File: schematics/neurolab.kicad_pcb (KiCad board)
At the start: 2 copper layers, 127 x 53.6 mm, 159 parts, among them J1 GS3, J10 GS3, J12 GS3, J13 GS3, J14 GS3, J15 GS3, J16 Channel, J17 External, J18 USB_OTG, J19 GS3, J2 GS3, J24 GS2, J3 GS3, J32 Bluetooth, J33 Reset Select, J34 GS2, J4 GS2, J5 GS2, J6 GS3, J7 GS3, J8 PowerOut, J9 GS3, Q1 2N7002, U1 ADP1720ARMZ-5, U10 OPA2111KP, U11 AD8422ARMZ, U12 OP4117, U13 OPA2111KP, U14 AD8422ARMZ, U15 OP4117, U16 AD7173, U17 ADR445BR, U18 Arduino, U2 ADP1720ARMZ-3.3, U3 AD8475, U4 AD8475, U5 MAX7480ESA+, U6 MAX7480ESA+, U7 MAX7480ESA+, U8 MAX7480ESA+, U9 TLC555CD, Y1 FA-20H

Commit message: optimize: final routing
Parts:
- removed J33: Reset Select, Connectors:GS3
- removed U18: Arduino, Pin_Headers:Pin_Header_Straight_2x12_Pitch2.54mm
- added J11: ProMini, Pin_Headers:Pin_Header_Straight_2x07_Pitch2.54mm, F.Cu at (179.8, 84.8)
- J32: footprint Pin_Headers:Pin_Header_Straight_1x06_Pitch2.54mm -> Pin_Headers:Pin_Header_Straight_1x04_Pitch2.54mm
- J34, J4, J5: moved to B.Cu
- moved J32 38.0 mm to (174.8, 80.9)
- moved J5 34.4 mm to (156.2, 101.9), turned to 0 degrees
- moved J4 34.0 mm to (156.4, 85.7), turned to 0 degrees
- moved J34 20.8 mm to (183.0, 104.9), turned to 0 degrees
- moved D2 19.3 mm to (183.4, 113.7)
- moved R44 17.6 mm to (183.4, 109.3), turned to 270 degrees
- moved R50 5.38 mm to (169.6, 79.8)
- moved R46 5.12 mm to (164.6, 82.2)
- moved R45 5.04 mm to (164.6, 79.8)
- moved R49 4.95 mm to (169.6, 82.2)
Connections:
- J32 pad 1: (no net) -> VCC
- J32 pad 2: VCC -> GND
- J32 pad 3: GND -> TxO
- J32 pad 4: TxO -> RxI
- R44 pad 1: Net-(D2-Pad2) -> Net-(J11-Pad12)
- R44 pad 2: Net-(R44-Pad2) -> Net-(D2-Pad2)
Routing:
- net Net-(J33-Pad1): track 80.7 -> 0.00 mm, vias 1 -> 0
- net AD3: track 110.3 -> 50.9 mm
- net Net-(J33-Pad3): track 49.6 -> 0.00 mm
- net GND: track 225.7 -> 186.9 mm, vias 57 -> 58
- net VCC: track 3.28 -> 39.2 mm, vias 0 -> 1
- net AD1: track 27.7 -> 62.5 mm, vias 0 -> 2
- net AD0: track 25.5 -> 59.0 mm, vias 0 -> 3
- net MOSI: track 5.02 -> 33.9 mm
- net CS: track 2.54 -> 29.0 mm, vias 0 -> 2
- net Net-(R44-Pad2): track 23.3 -> 0.00 mm, vias 2 -> 0
- net SCL: track 0.00 -> 19.6 mm, vias 0 -> 2
- net AD2: track 56.5 -> 40.5 mm, vias 0 -> 2
- net /ADConverter/DI: track 5.90 -> 20.1 mm
- net /ADConverter/SCL: track 6.64 -> 19.7 mm
- net Net-(J11-Pad12): track 0.00 -> 11.9 mm
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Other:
- board size 127 x 53.6 mm -> 93.4 x 38.3 mm

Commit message: feat: schematics and readme update
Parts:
- added C64: 100u, Capacitors_Tantalum_SMD:CP_Tantalum_Case-C_EIA-6032-28_Reflow, F.Cu at (96.8, 118.6)
- added C65: 100u, Capacitors_Tantalum_SMD:CP_Tantalum_Case-C_EIA-6032-28_Reflow, F.Cu at (96.7, 130.4)
- added C66: 100u, Capacitors_Tantalum_SMD:CP_Tantalum_Case-C_EIA-6032-28_Reflow, F.Cu at (105.3, 130.4)
- added C67: 100u, Capacitors_Tantalum_SMD:CP_Tantalum_Case-C_EIA-6032-28_Reflow, F.Cu at (105.3, 118.7)
- added C68: 100u, Capacitors_Tantalum_SMD:CP_Tantalum_Case-C_EIA-6032-28_Reflow, F.Cu at (113.9, 130.4)
- added C69: 100u, Capacitors_Tantalum_SMD:CP_Tantalum_Case-C_EIA-6032-28_Reflow, F.Cu at (113.9, 118.6)
- added G***: LOGO, Neuro:Logo, F.Cu at (173.6, 90.7)
- added G***: LOGO, Neuro:QR, B.Cu at (130.2, 97.8)
- added JP1: VoltOut, Connectors:GS3, B.Cu at (114.0, 124.4)
- added JP2: VVV, Connectors:GS3, B.Cu at (109.2, 124.4)
- added REF***: ESD-Logo_8.9x8mm_SilkScreen, Symbols:ESD-Logo_8.9x8mm_SilkScreen, B.Cu at (170.4, 111.0)
- added REF***: OSHW-Logo_5.7x6mm_SilkScreen, Symbols:OSHW-Logo_5.7x6mm_SilkScreen, B.Cu at (100.4, 127.3)
- added REF***: WEEE-Logo_5.6x8mm_SilkScreen, Symbols:WEEE-Logo_5.6x8mm_SilkScreen, B.Cu at (179.8, 111.7)
- added U18: TC1240A, TO_SOT_Packages_SMD:SOT-23-6, F.Cu at (96.8, 124.6)
- added U19: TC1240A, TO_SOT_Packages_SMD:SOT-23-6, F.Cu at (105.3, 124.6)
- added U20: 7660, Housings_SOIC:SOIC-8_3.9x4.9mm_Pitch1.27mm, F.Cu at (113.9, 124.5)
- J16: moved to B.Cu
- J8: value PowerOut -> 5.5V; footprint Pin_Headers:Pin_Header_Straight_2x02_Pitch2.54mm -> Pin_Headers:Pin_Header_Straight_1x01_Pitch2.54mm
- moved J8 24.3 mm to (117.1, 112.0)
- moved J16 12.7 mm to (95.7, 90.7)
- moved J18 1.50 mm to (94.6, 83.0)
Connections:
- J16 pad 1: /Amplifier Block 2/IN+ -> /Amplifier Block 1/IN-
- J16 pad 2: /Amplifier Block 2/IN- -> /Amplifier Block 1/IN+
- J16 pad 5: /Amplifier Block 1/IN+ -> /Amplifier Block 2/IN-
- J16 pad 6: /Amplifier Block 1/IN- -> /Amplifier Block 2/IN+
- J8 pad 1: -12V -> +5.5V
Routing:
- net +5V: track 192.1 -> 264.2 mm, vias 14 -> 17
- net Net-(C65-Pad1): track 0.00 -> 32.8 mm, vias 0 -> 1
- net -12V: track 152.2 -> 175.0 mm, vias 7 -> 9
- net +5.5V: track 148.7 -> 126.4 mm, vias 3 -> 2
- net Net-(C67-Pad1): track 0.00 -> 17.4 mm, vias 0 -> 1
- net Net-(C21-Pad3): track 34.7 -> 20.1 mm, vias 0 -> 1
- net Net-(C20-Pad3): track 33.2 -> 21.1 mm, vias 0 -> 1
- net +12V: track 162.0 -> 173.2 mm
- net Net-(C66-Pad1): track 0.00 -> 8.05 mm
- net Net-(C64-Pad2): track 0.00 -> 8.05 mm
- net Net-(C64-Pad1): track 0.00 -> 6.05 mm
- net Net-(C66-Pad2): track 0.00 -> 5.99 mm
- net Net-(C68-Pad1): track 0.00 -> 4.95 mm
- net Net-(JP2-Pad2): track 0.00 -> 4.89 mm, vias 0 -> 1
- net GND: track 186.9 -> 182.4 mm, vias 58 -> 64
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- added copper zone on F.Cu, net (none)
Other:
- board size 93.4 x 38.3 mm -> 93.6 x 55 mm
- board text added: "+12 OUT 5.5V"
- board text added: "+5.5V"
- board text added: "+5V"
- board text added: "+5V VCO 5.5V"
- board text added: "AD0"
- board text added: "AD1"
- board text added: "AD2"
- board text added: "AD2 GND"
- board text added: "AD3"
- board text added: "AD3 CPG"
- board text added: "AVC VCC"
- board text added: "CLK"
- board text added: "CS"
- board text added: "GND"
- board text added: "I1+ I1- GND GND I2+ I2-"
- board text added: "ICL CLK ECL"
- board text added: "IN+ IN+ OUT"
- board text added: "IN+ OU- OUT"
- board text added: "IN- OU- OUT"
- board text added: "LED"
- board text added: "MISO"
- board text added: "MOSI"
- board text added: "NeuroLab V1.0 Experimental Design"
- board text added: "OUT IN- IN-"
- board text added: "Rx"
- board text added: "SCL"
- board text added: "Sx1 +12 Sx2"
- board text added: "Tx"
- board text added: "USB +5V EXT"
- board text added: "VCC"
- board text added: "VCO A13"
- board text added: "VLO OUT VLH"

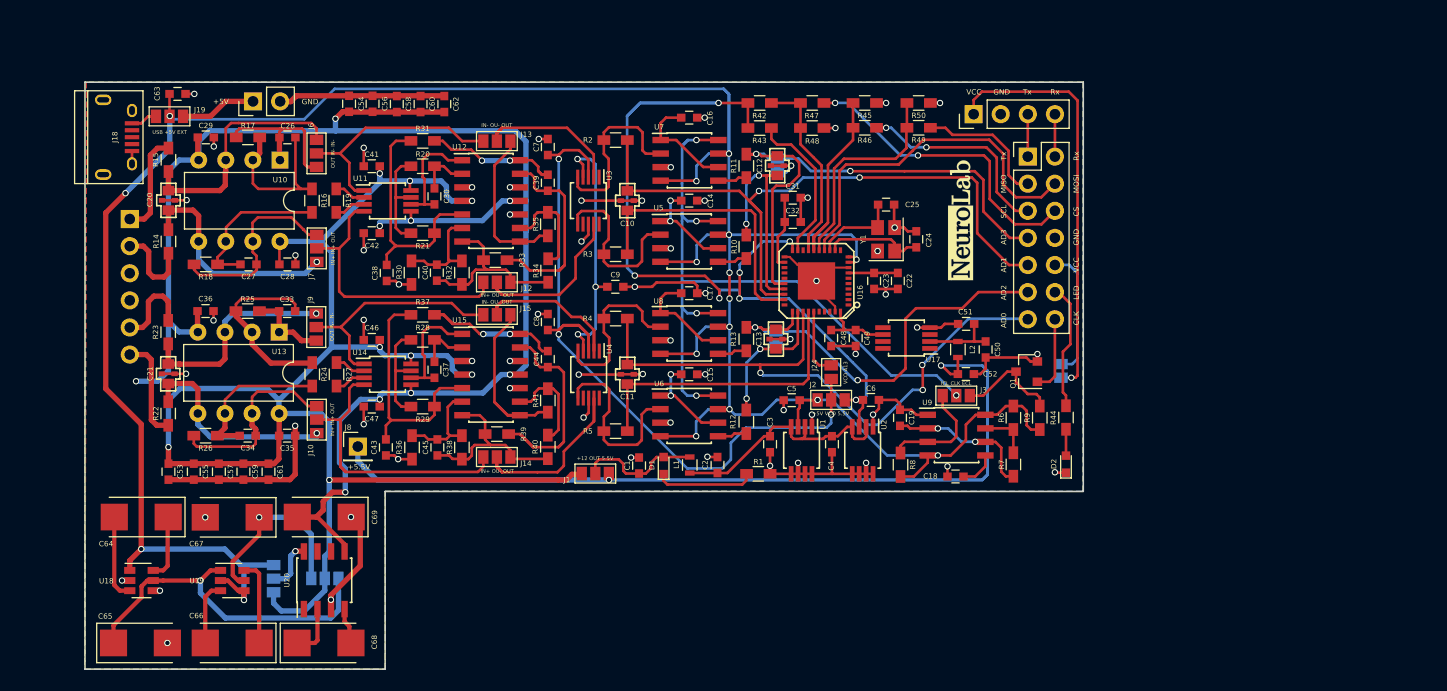
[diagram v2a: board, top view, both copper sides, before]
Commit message: Optimized Routing and Fixed DRC
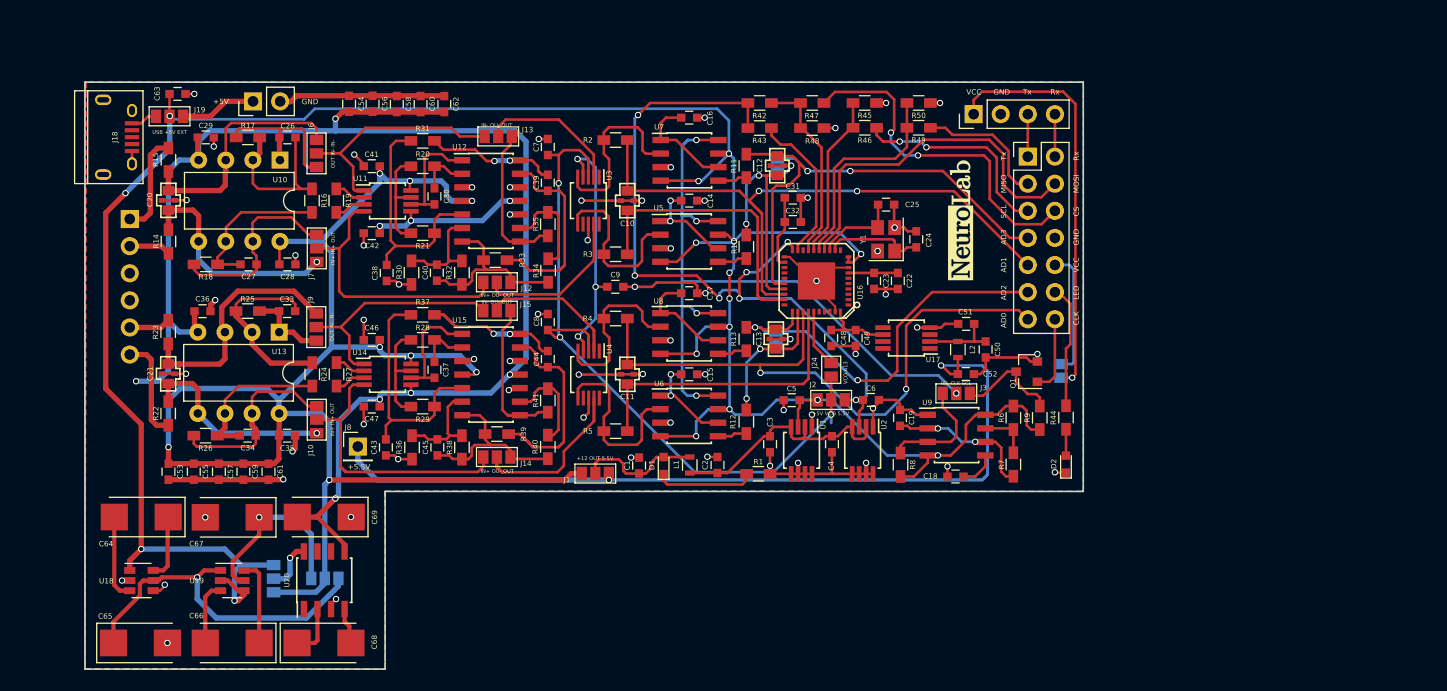
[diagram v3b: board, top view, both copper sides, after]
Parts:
- moved J13 0.46 mm to (130.2, 83.0)
- moved J15 0.39 mm to (130.1, 99.3)
- moved C36 0.29 mm to (102.5, 99.3)
- moved J24 0.22 mm to (161.4, 104.8)
- moved J3 0.21 mm to (173.2, 107.0)
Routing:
- net GND: track 182.4 -> 163.5 mm, vias 64 -> 65
- net +3V: track 88.4 -> 75.9 mm
- net -12V: track 175.0 -> 165.2 mm
- net +5V: track 264.2 -> 254.4 mm
- net +12V: track 173.2 -> 164.3 mm
- net VCCIO: track 74.6 -> 70.3 mm
- net /ADConverter/SCL: track 19.7 -> 15.4 mm
- net /Amplifier Block 1/IN+: track 7.99 -> 3.91 mm
- net /Amplifier Block 2/IN-: track 8.01 -> 3.98 mm
- net AD1: track 62.5 -> 58.7 mm
- net AD3: track 50.9 -> 47.2 mm
- net CS: track 29.0 -> 32.6 mm
- net Net-(C21-Pad1): track 19.9 -> 22.9 mm, vias 1 -> 0
- net Net-(J15-Pad3): track 18.3 -> 15.9 mm
- net AD0: track 59.0 -> 61.1 mm, vias 3 -> 2
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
